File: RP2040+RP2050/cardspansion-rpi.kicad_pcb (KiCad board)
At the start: 2 copper layers, 22 x 30 mm, 4 parts, among them J1 M2-E 2230, U1 RP2350-Tiny

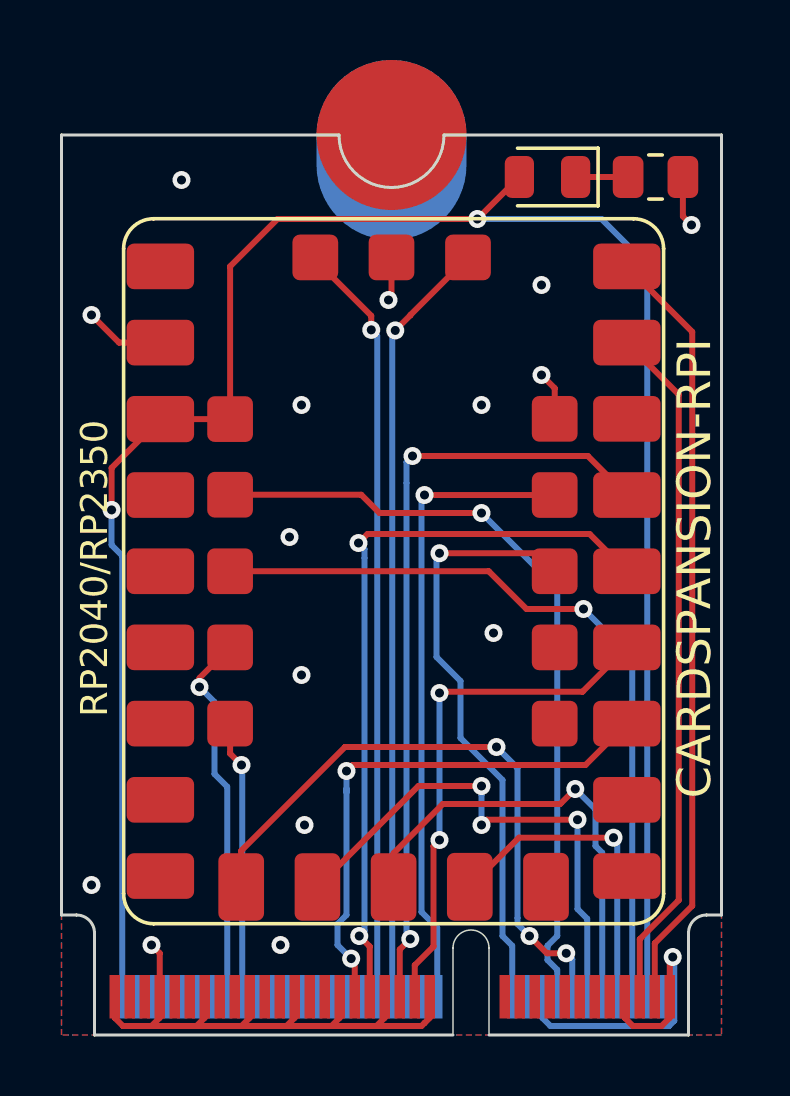
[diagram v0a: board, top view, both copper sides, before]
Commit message: Fix cardspansion-rpi I2S wiring
I2S-SDIN and I2S-SDOUT nets were switched around
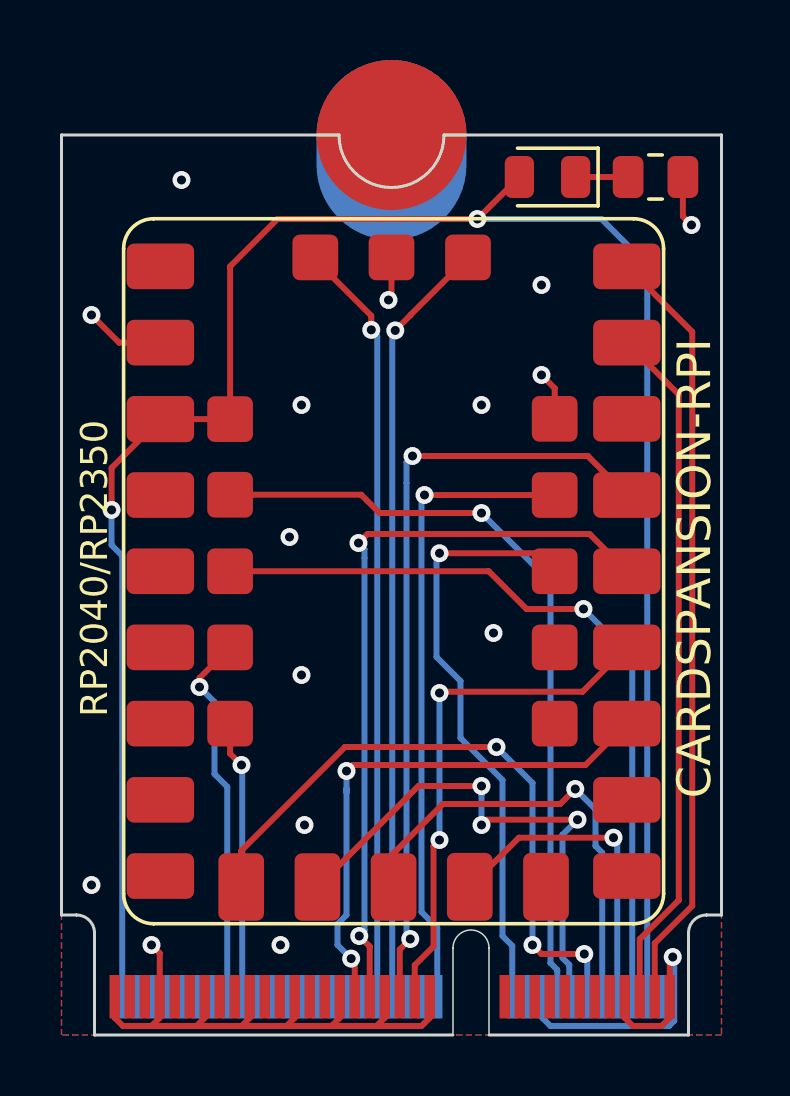
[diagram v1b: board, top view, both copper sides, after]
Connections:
- J1 pad 12: /I2S-SDOUT -> /I2S-SDIN
- J1 pad 14: /I2S-SDIN -> /I2S-SDOUT
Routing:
- net /I2S-SDIN: track 20.9 -> 21.6 mm
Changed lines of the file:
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@@
 			(size 0.35 1.45)
 			(layers "B.Cu" "B.Mask")
-			(net 34 "/I2S-SDOUT")
+			(net 15 "/I2S-SDIN")
 			(pinfunction "PCM_IN/I2S_SD_IN")
 			(pintype "input")
@@
 			(size 0.35 1.45)
 			(layers "B.Cu" "B.Mask")
-			(net 15 "/I2S-SDIN")
+			(net 34 "/I2S-SDOUT")
 			(pinfunction "PCM_OUT/I2S_SD_OUT")
 			(pintype "output")
@@
 	)
 	(segment
-		(start 77.824265 108.275735)
-		(end 77.175735 108.275735)
+		(start 76.7 108)
+		(end 76.699 108)
+		(width 0.2)
+		(layer "F.Cu")
+		(net 15)
+	)
+	(segment
+		(start 77 108.3)
+		(end 76.7 108)
 		(width 0.2)
 		(layer "F.Cu")
@@
 	)
 	(segment
-		(start 77.175735 108.275735)
-		(end 76.6 107.7)
-		(width 0.2)
-		(layer "F.Cu")
-		(net 15)
-	)
-	(segment
 		(start 70.450057 101.4)
 		(end 66.99 104.860057)
@@
 		(net 15)
 	)
+	(segment
+		(start 78.425 108.3)
+		(end 77 108.3)
+		(width 0.2)
+		(layer "F.Cu")
+		(net 15)
+	)
 	(via
 		(at 75.5 101.4)
@@
 	)
 	(via
-		(at 76.6 107.7)
+		(at 76.699 108)
 		(size 0.6)
 		(drill 0.3)
@@
 	)
 	(via
-		(at 77.824265 108.275735)
+		(at 78.425 108.3)
 		(size 0.6)
 		(drill 0.3)
@@
 	)
 	(segment
-		(start 78.025 108.47647)
-		(end 77.824265 108.275735)
+		(start 76.699 102.599)
+		(end 75.5 101.4)
 		(width 0.2)
 		(layer "B.Cu")
@@
 	)
 	(segment
-		(start 76.2 107.3)
-		(end 76.2 107.1)
+		(start 78.525 108.4)
+		(end 78.525 109.725)
 		(width 0.2)
 		(layer "B.Cu")
@@
 	)
 	(segment
-		(start 76.2 102.1)
-		(end 75.5 101.4)
+		(start 78.425 108.3)
+		(end 78.525 108.4)
 		(width 0.2)
 		(layer "B.Cu")
@@
 	)
 	(segment
-		(start 76.6 107.7)
-		(end 76.5 107.6)
-		(width 0.2)
-		(layer "B.Cu")
-		(net 15)
-	)
-	(segment
-		(start 76.5 107.6)
-		(end 76.2 107.3)
-		(width 0.2)
-		(layer "B.Cu")
-		(net 15)
-	)
-	(segment
-		(start 76.2 107.1)
-		(end 76.2 102.1)
-		(width 0.2)
-		(layer "B.Cu")
-		(net 15)
-	)
-	(segment
-		(start 78.025 109.725)
-		(end 78.025 108.47647)
+		(start 76.699 108)
+		(end 76.699 102.599)
 		(width 0.2)
 		(layer "B.Cu")
@@
 	)
 	(segment
-		(start 77.525 107.7)
-		(end 77.525 96.125)
+		(start 77.299 95.901)
+		(end 77.3 95.9)
 		(width 0.2)
 		(layer "B.Cu")
@@
 	)
 	(segment
-		(start 77.525 96.125)
+		(start 77.525 108.825)
+		(end 77.299 108.599)
+		(width 0.2)
+		(layer "B.Cu")
+		(net 18)
+	)
+	(segment
+		(start 77.3 95.9)
 		(end 75.001 93.601)
-		(width 0.2)
-		(layer "B.Cu")
-		(net 18)
-	)
-	(segment
-		(start 77.525 108.825)
-		(end 77.2 108.5)
-		(width 0.2)
-		(layer "B.Cu")
-		(net 18)
-	)
-	(segment
-		(start 77.2 108.025)
-		(end 77.525 107.7)
 		(width 0.2)
 		(layer "B.Cu")
@@
 	)
 	(segment
-		(start 77.2 108.5)
-		(end 77.2 108.025)
+		(start 77.299 108.599)
+		(end 77.299 95.901)
 		(width 0.2)
 		(layer "B.Cu")
@@
 	)
 	(segment
-		(start 78.525 109.725)
-		(end 78.525 107.125)
-		(width 0.2)
-		(layer "B.Cu")
-		(net 34)
-	)
-	(segment
 		(start 75 104)
 		(end 75 103)
@@
 	)
 	(segment
-		(start 78.2 106.8)
+		(start 78.025 109.725)
+		(end 77.926 109.626)
+		(width 0.2)
+		(layer "B.Cu")
+		(net 34)
+	)
+	(segment
+		(start 77.7 104.323)
 		(end 78.2 103.823)
 		(width 0.2)
@@
 	)
 	(segment
-		(start 78.525 107.125)
-		(end 78.2 106.8)
-		(width 0.2)
-		(layer "B.Cu")
+		(start 77.7 108.4329)
+		(end 77.7 104.323)
+		(width 0.2)
+		(layer "B.Cu")
+		(net 34)
+	)
+	(segment
+		(start 77.926 108.6589)
+		(end 77.7 108.4329)
+		(width 0.2)
+		(layer "B.Cu")
+		(net 34)
+	)
+	(segment
+		(start 77.926 109.626)
+		(end 77.926 108.6589)
+		(width 0.2)
+		(layer "B.Cu")
